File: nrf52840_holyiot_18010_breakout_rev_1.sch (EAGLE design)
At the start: 22 parts, among them IC1 MMA8652FCR1, IC2 HOLYIOT_18010, J1 NO_BOM, J2 NO_BOM

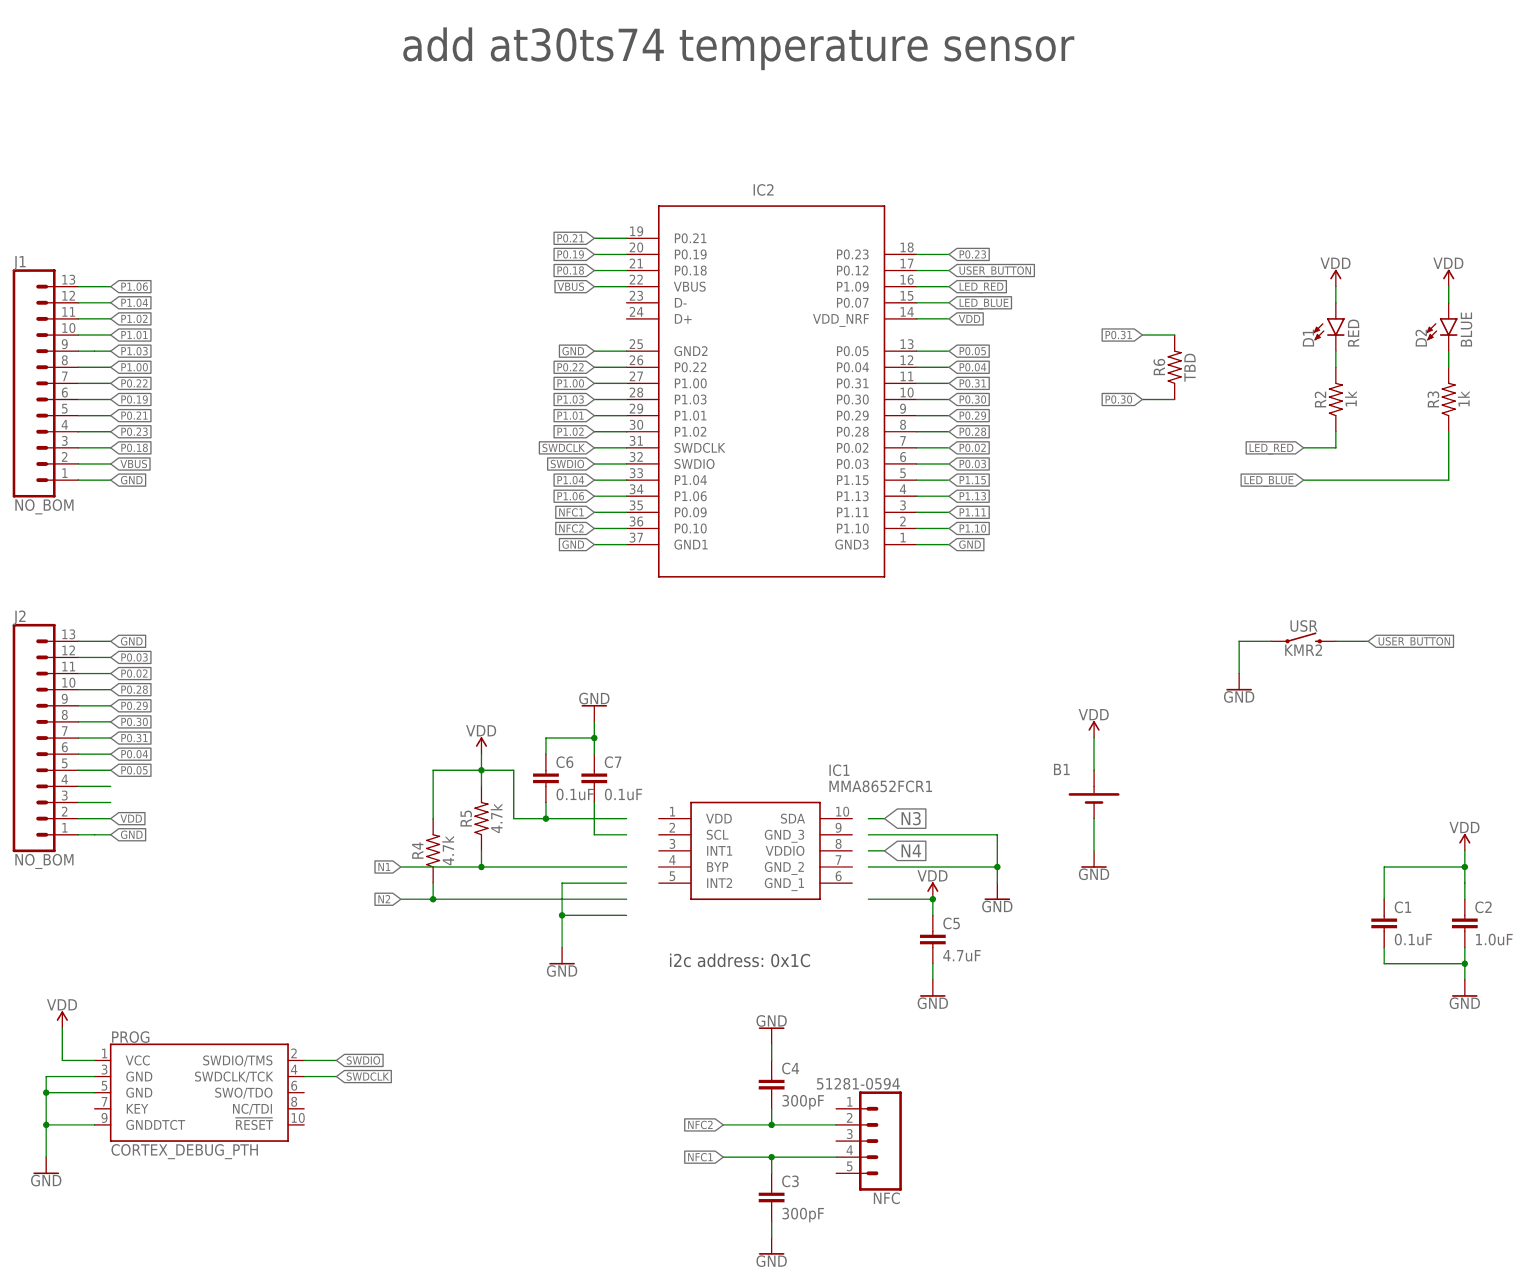
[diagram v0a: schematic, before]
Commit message: added temp sensor, first draft routing done
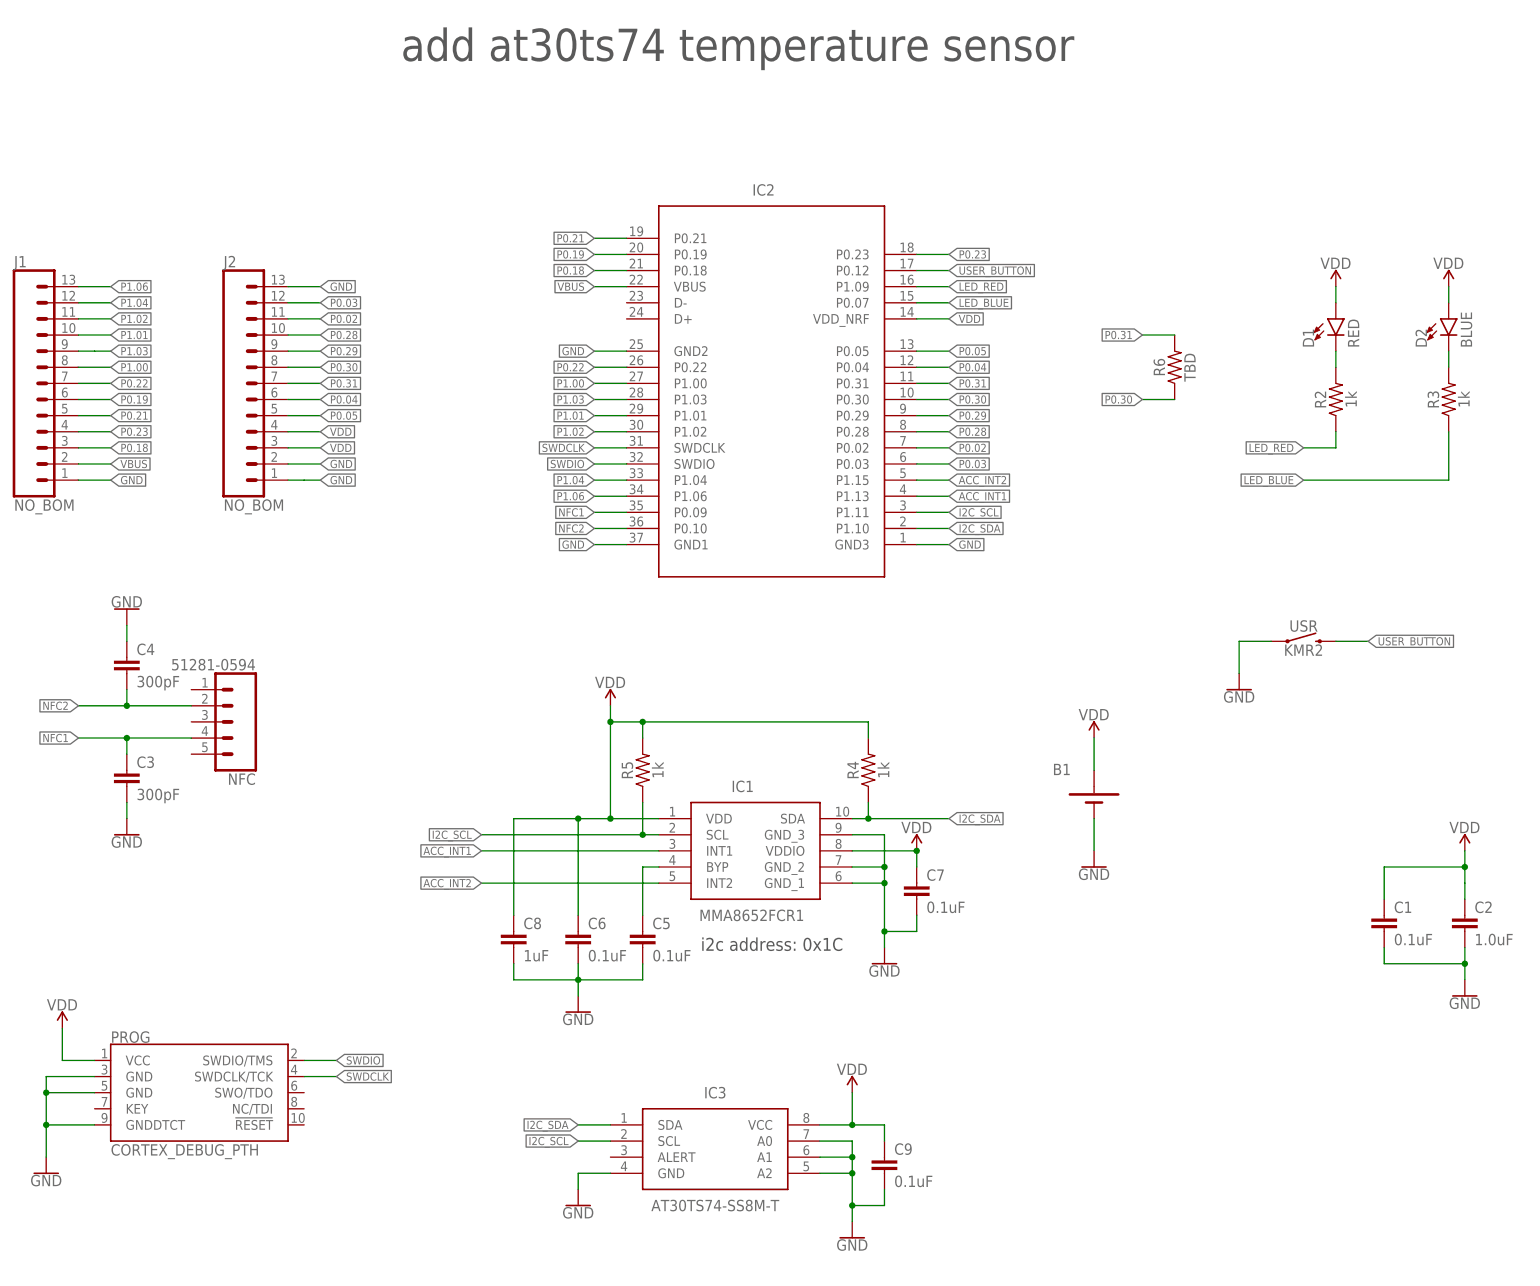
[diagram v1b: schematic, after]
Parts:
- added C8: 1uF, Inventas-Passives:CAP-6.3V-20%-0402
- added C9: 0.1uF, Inventas-Passives:CAP-6.3V-20%-0402
- added IC3: AT30TS74-SS8M-T, Inventas-IC:AT30TS74-SS8M-T
- C5: value 4.7uF -> 0.1uF; device Inventas-Passives:CAP-6.3V-20%-0603 -> Inventas-Passives:CAP-6.3V-20%-0402
- J1, J2: device SparkFun-Connectors:CONN_13 -> Inventas-Connectors:CONN_13NO_SILK
- R4, R5: value 4.7k -> 1k
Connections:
- removed net N$13: J2.4
- removed net N$14: J2.3
- removed net N$6: C7.2
- removed net N1: R5.1
- removed net N2: R4.1
- removed net P1.10: IC2.P1.10
- removed net P1.11: IC2.P1.11
- removed net P1.13: IC2.P1.13
- removed net P1.15: IC2.P1.15
- new net ACC_INT1: IC1.INT1, IC2.P1.13
- new net ACC_INT2: IC1.INT2, IC2.P1.15
- new net I2C_SCL: IC1.SCL, IC2.P1.11, IC3.SCL, R5.1
- new net I2C_SDA: IC1.SDA, IC2.P1.10, IC3.SDA, R4.1
- new net N$3: C5.1, IC1.BYP
- net GND: now also C6.2, C7.2, C8.2, C9.2, IC1.GND_1, IC1.GND_2, IC1.GND_3, IC3.A0, IC3.A1, IC3.A2, IC3.GND, J2.2; no longer C6.1, C7.1
- net VDD: now also C6.1, C7.1, C8.1, C9.1, IC1.VDD, IC1.VDDIO, IC3.VCC, J2.3, J2.4; no longer C5.1, C6.2, J2.2
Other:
- moved on the sheet: C3, C4, C5, C6, C7, J2, NFC, R4, R5

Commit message: small fixes when adding 3D packages
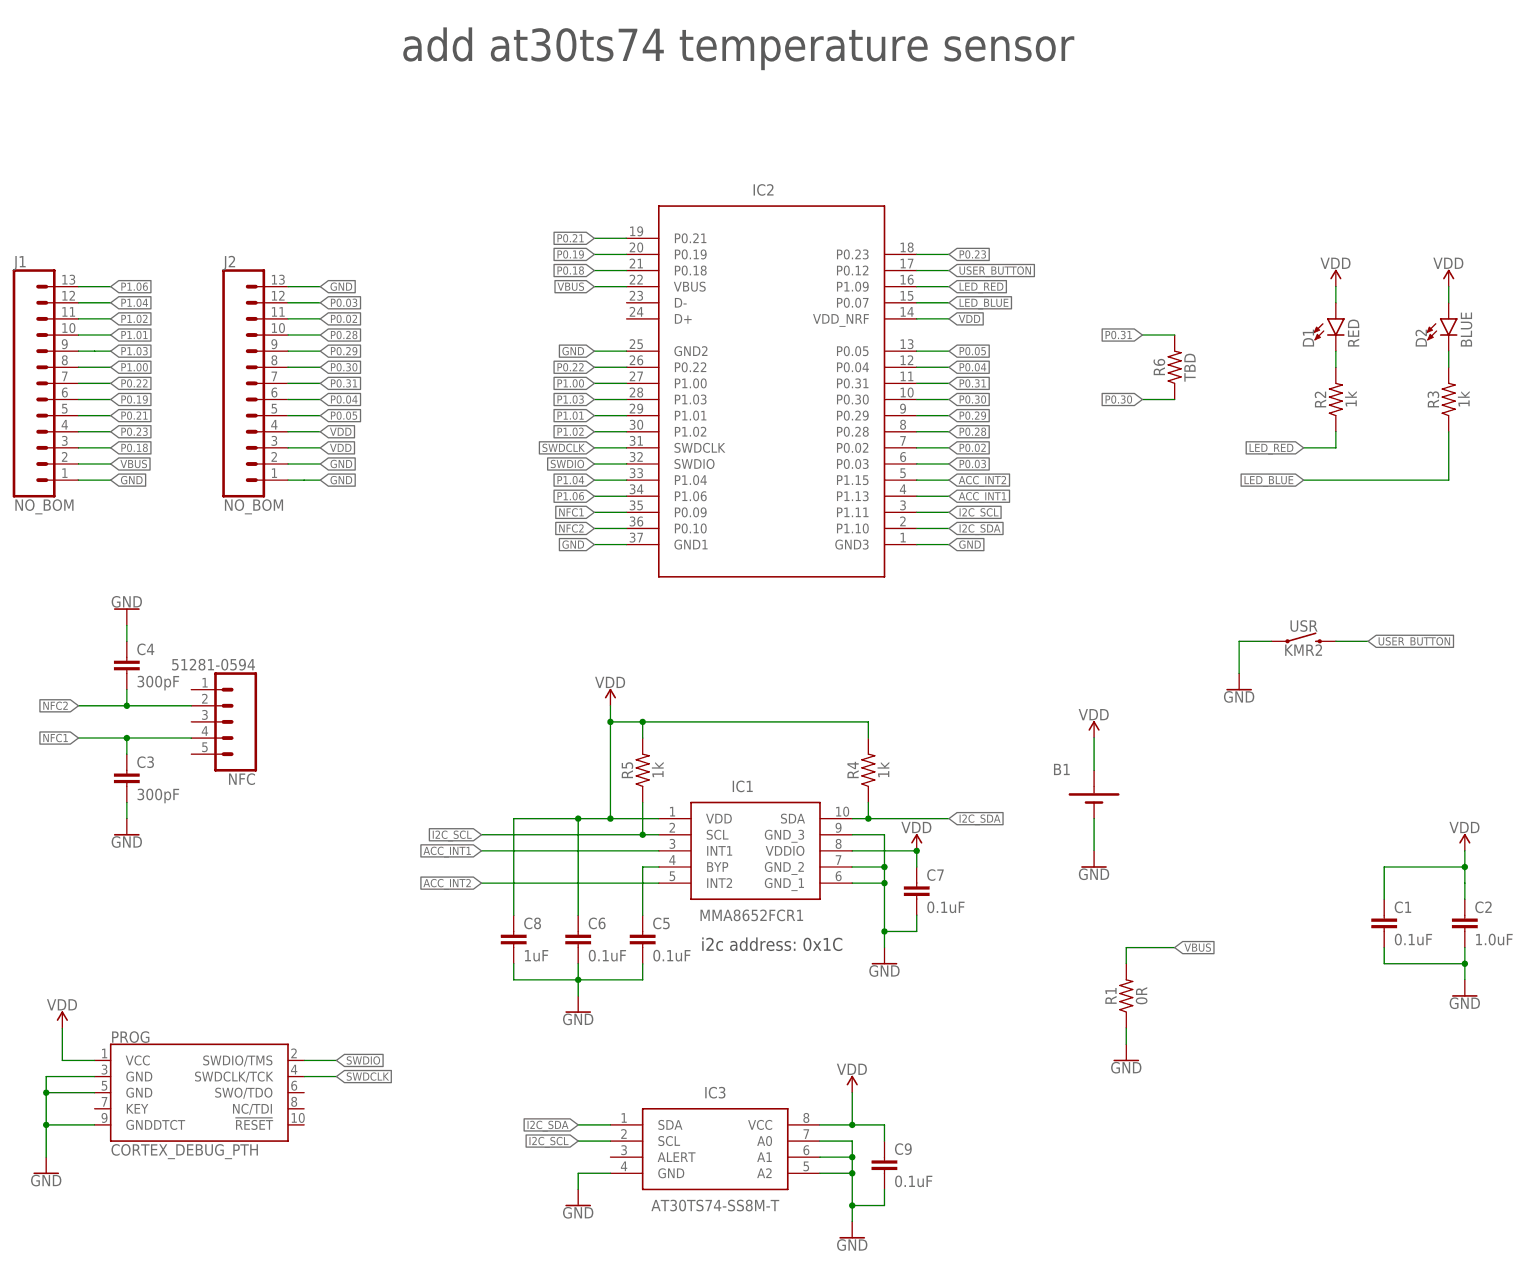
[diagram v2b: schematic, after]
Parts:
- added R1: 0R, Inventas-Passives:RES-0.063W-5%-0402
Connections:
- net GND: now also R1.1
- net VBUS: now also R1.2
